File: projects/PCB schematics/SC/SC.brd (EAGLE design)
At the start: 99.1 x 99.1 mm, 76 parts, among them X1 5566-10, X2 5566-2, X4 5566-12

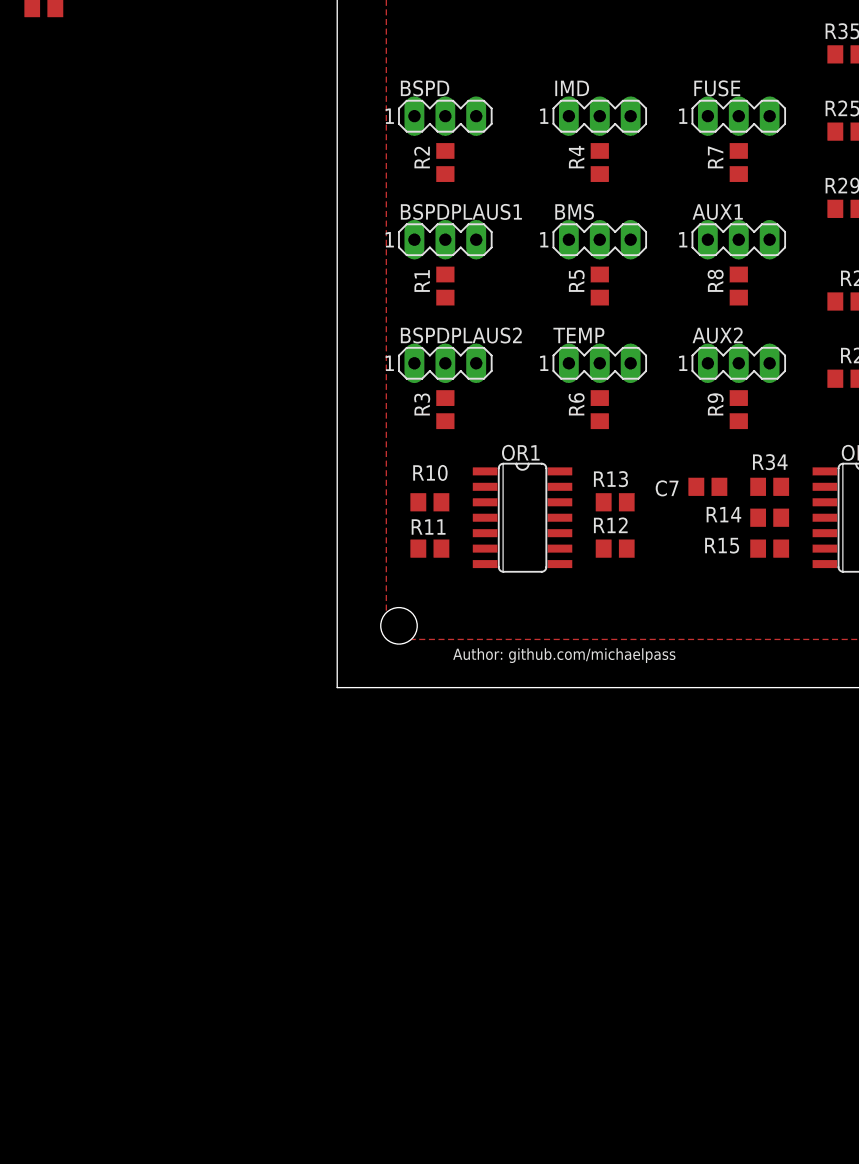
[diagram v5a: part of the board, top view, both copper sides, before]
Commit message: TEMP - Initial board placement; Horizontal redo.
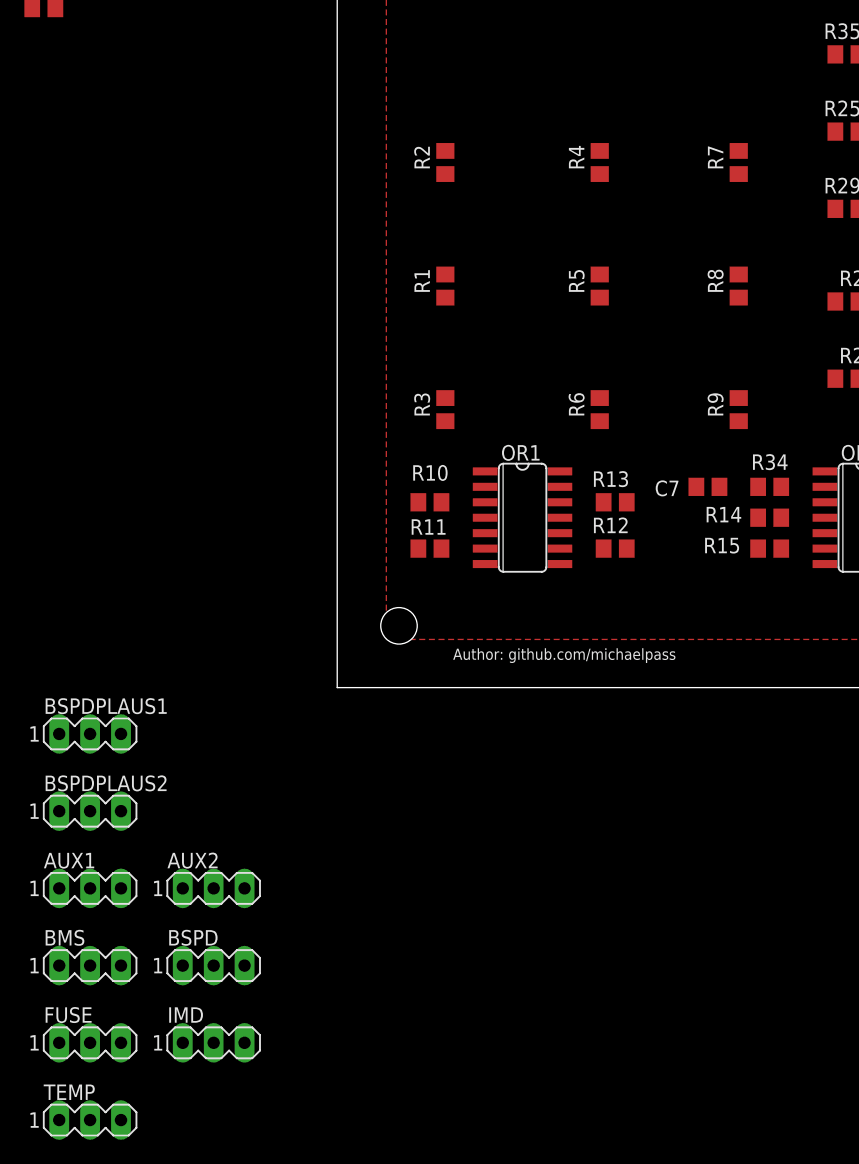
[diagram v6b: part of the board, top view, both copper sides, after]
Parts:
- moved FUSE 93.0 mm to (-20.3, -29.2)
- moved IMD 82.5 mm to (-10.2, -29.2)
- moved AUX1 75.4 mm to (-20.3, -16.5)
- moved TEMP 75.0 mm to (-20.3, -35.6)
- moved BMS 72.9 mm to (-20.3, -22.9)
- moved BSPD 72.4 mm to (-10.2, -22.9)
- moved AUX2 61.1 mm to (-10.2, -16.5)
- moved BSPDPLAUS1 50.0 mm to (-20.3, -3.81)
- moved BSPDPLAUS2 47.0 mm to (-20.3, -10.2)
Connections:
- new net GND1: AUX1.3, AUX2.3, BMS.3, BSPDPLAUS2.3, FUSE.3, IMD.3, TEMP.3
- new net N$20: BSPD.3
- net AUX1_B: no longer BUF2.4
- net AUX2_B: no longer BUF2.6
- net BMSFAULT_B: no longer BUF1.10
- net BSPDFAULT_B: no longer BUF1.2
- net BSPDPLAUS1_B: no longer BUF1.4
- net BSPDPLAUS1_O: no longer BSPDPLAUS1.2
- net BSPDPLAUS2_B: no longer BUF1.6
- net FUSEFAULT_B: no longer BUF2.2
- net GND: no longer AUX1.3, AUX2.3, BMS.3, BSPD.3, BSPDPLAUS1.3, BSPDPLAUS2.3, FUSE.3, IMD.3, TEMP.3
- net IMDFAULT_B: no longer BUF1.8
- net TEMPFAULT_B: no longer BUF1.12

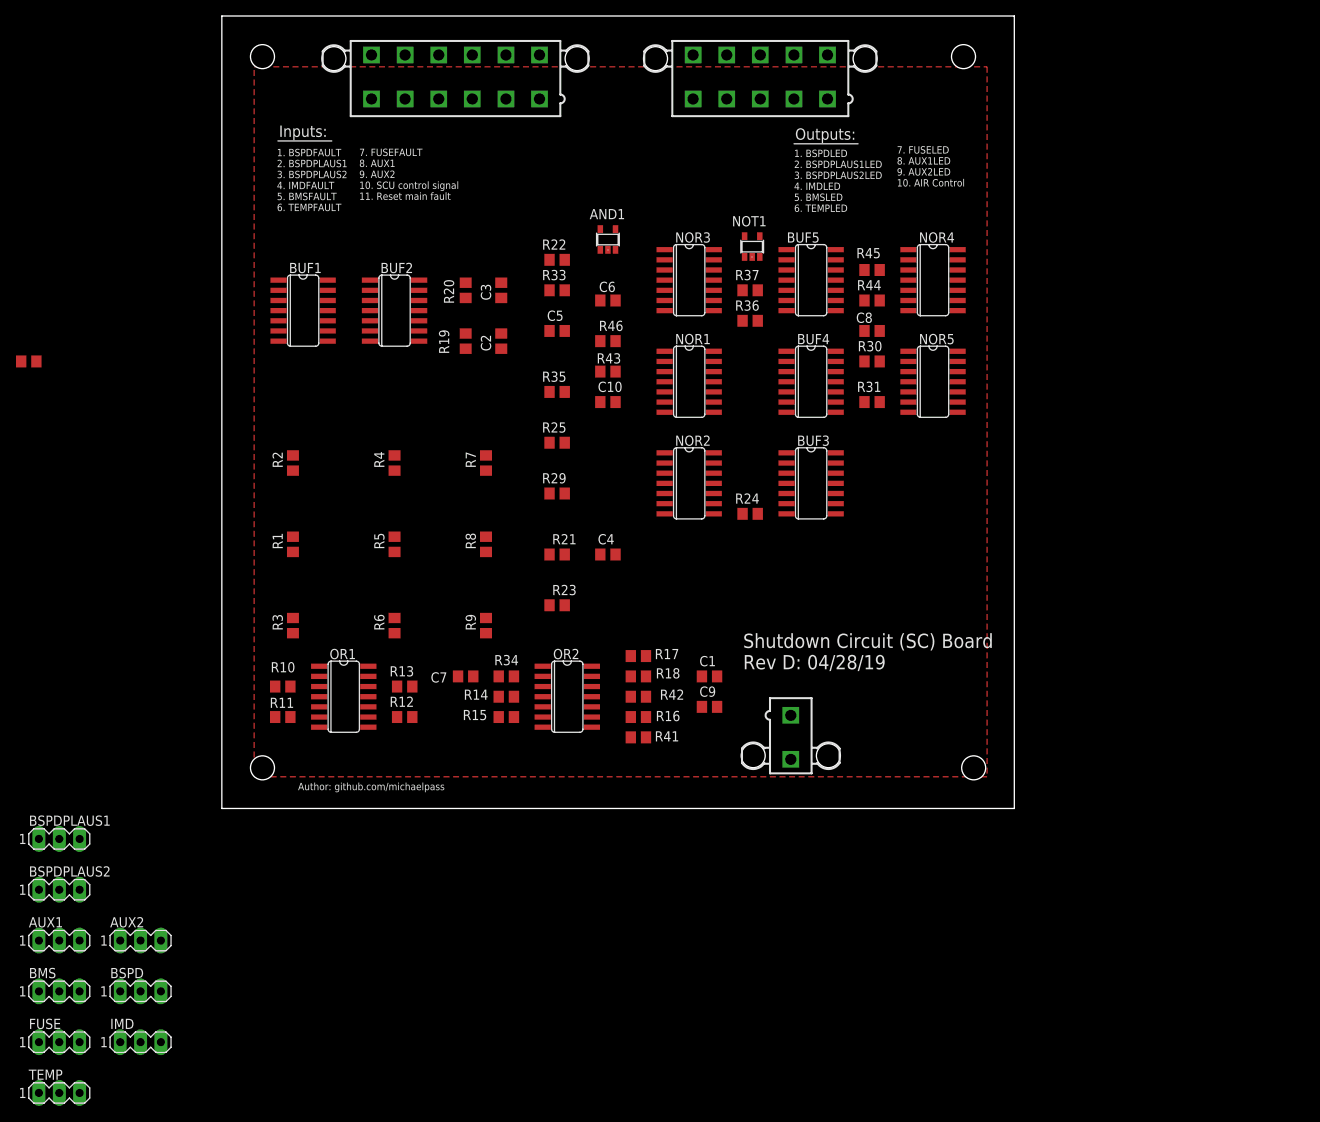
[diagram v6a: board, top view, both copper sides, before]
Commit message: SC - Hand routing. Ready for autorouter.
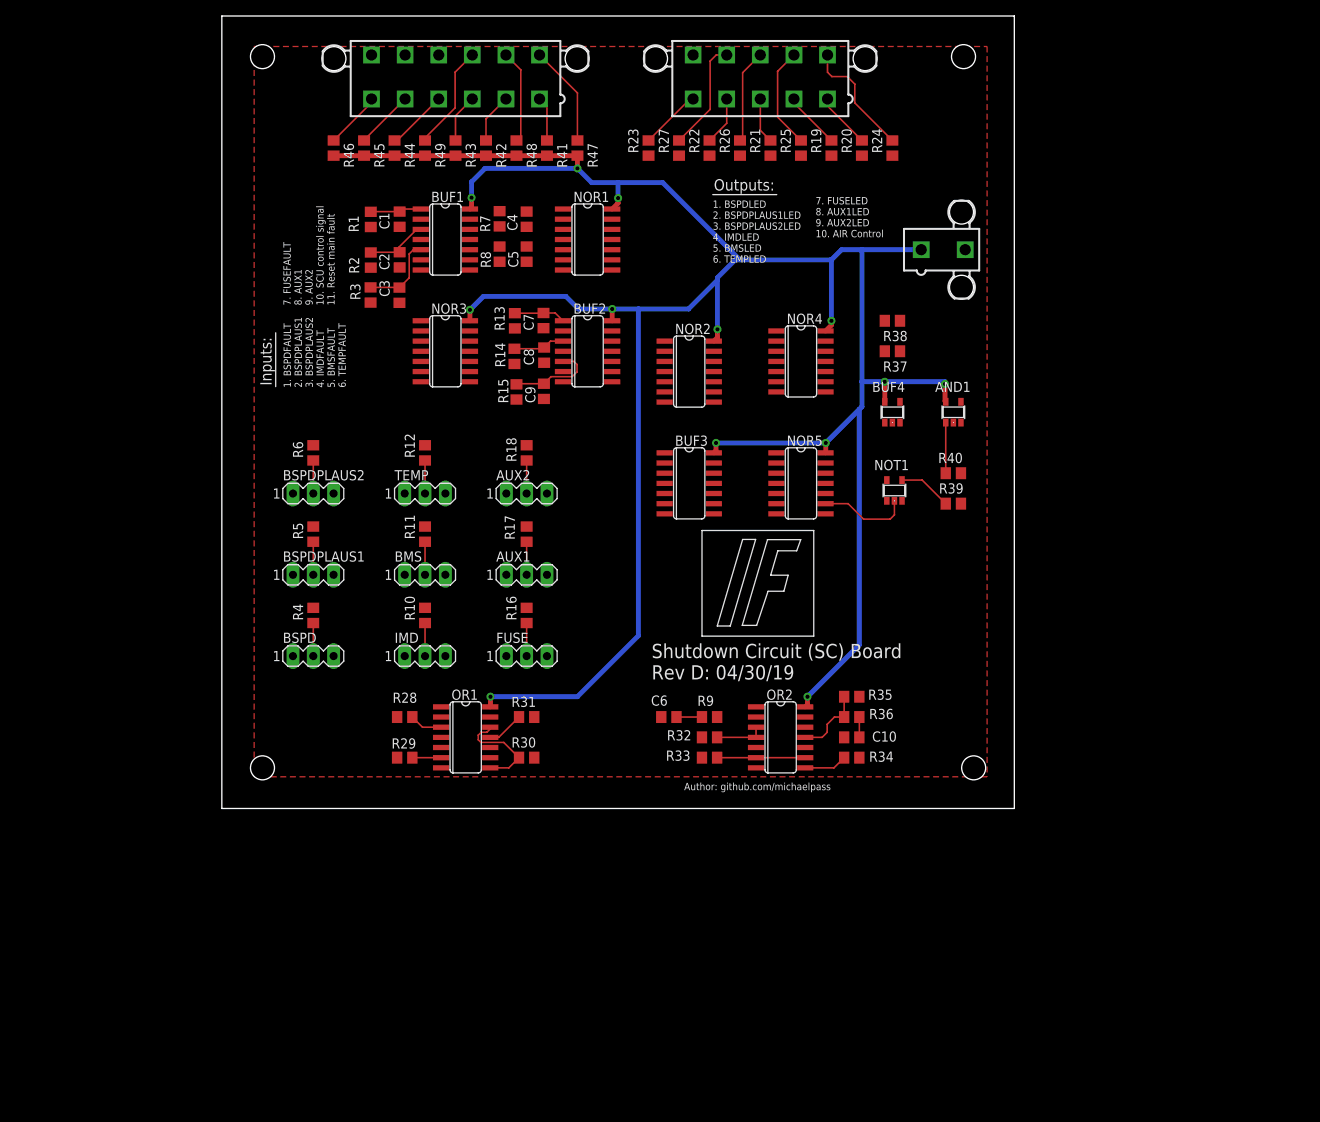
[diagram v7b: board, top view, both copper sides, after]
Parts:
- removed BUF5: 74HC7014, IowaFormula:SO14
- removed X4: 5566-12, con-molex:5566-12
- added R26, R27, R28, R38, R39, R40: 10k, rcl:R0805
- added R47, R48, R49: 47k, rcl:R0805
- added X3: 5566-10, con-molex:5566-10
- BUF4: value 74HC7014 -> 74AUC1G17DBV; device IowaFormula:SO14 -> 74xx-little-us:SOT23-5
- C1, C2, C3, C4, C5, C6, C7, C8, C9: value 1 uF -> 1u
- NOR1, NOR2, NOR3, NOR4, NOR5: value 74LS02D -> 74ALS02D
- R1, R13, R14, R15, R2, R3, R44, R45, R46, R7, R8, R9: value 10k -> 47k
- R18, R19, R20, R21, R32, R33, R34: value 50k -> 10k
- R36: value 10k -> 50k
- R41, R42, R43: value 50k -> 47k
- X1: value 5566-10 -> 5566-2; device con-molex:5566-10 -> con-molex:5566-2
- X2: value 5566-2 -> 5566-12; device con-molex:5566-2 -> con-molex:5566-12
- moved R32 97.2 mm to (61.0, 8.89), turned to 0 degrees
- moved X2 92.6 mm to (29.2, 91.4), turned to 0 degrees
- moved TEMP 87.8 mm to (25.4, 39.4)
- moved FUSE 75.8 mm to (38.1, 19.1)
- moved R41 74.5 mm to (40.6, 82.5), turned to 270 degrees
- moved AUX1 74.2 mm to (38.1, 29.2)
- moved AUX2 73.8 mm to (38.1, 39.4)
- moved R42 71.2 mm to (33.0, 82.5), turned to 270 degrees
- moved BMS 69.3 mm to (25.4, 29.2)
- moved C1 69.0 mm to (22.2, 73.7), turned to 270 degrees
- moved R30 65.7 mm to (38.1, 6.35)
- moved R45 65.3 mm to (17.8, 82.5), turned to 270 degrees
- moved R44 62.7 mm to (21.6, 82.5), turned to 270 degrees
- moved R33 61.4 mm to (61.0, 6.35), turned to 0 degrees
- moved IMD 59.9 mm to (25.4, 19.1)
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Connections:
- removed net AUX1_O: AUX1.2, OR2.10, R8.2
- removed net AUX2_O: AUX2.2, OR2.13, R9.2
- removed net BMSFAULT_O: BMS.2, OR1.13, R5.2
- removed net BSPDFAULT_O: BSPD.2, OR1.1, R2.2
- removed net BSPDPLAUS1_O: OR1.2, R1.2
- removed net BSPDPLAUS2_O: BSPDPLAUS2.2, OR1.5, R3.2
- removed net FUSEFAULT_O: FUSE.2, OR2.5, R7.2
- removed net GND1: AUX1.3, AUX2.3, BMS.3, BSPDPLAUS2.3, FUSE.3, IMD.3, TEMP.3
- removed net IMDFAULT_O: IMD.2, OR1.10, R4.2
- removed net N$20: BSPD.3
- removed net TEMPFAULT_O: OR2.2, R6.2, TEMP.2
- net AIR_CONTROL: now also X3.10; no longer X1.10
- net AUX1: now also R14.1, R48.1, X2.8; no longer R42.1, X4.8
- net AUX1_B: now also BUF2.4
- net AUX1_LED: now also BUF3.10, OR2.10, R26.2, X3.8; no longer BUF2.3, BUF4.2, X1.8
- net AUX2: now also R15.1, R49.1, X2.9; no longer R43.1, X4.9
- net AUX2_B: now also BUF2.6
- net AUX2_LED: now also BUF3.12, OR2.13, R27.2, X3.9; no longer BUF2.5, BUF4.6, X1.9
- net BMSFAULT: now also R45.1, R8.1, X2.5; no longer R33.1, X4.5
- net BMSFAULT_B: now also BUF1.10
- net BMSFAULT_LED: now also BUF3.4, OR1.13, R23.2, X3.5; no longer BUF1.11, BUF5.2, X1.5
- net BSPDFAULT: now also R1.1, R41.1, X2.1; no longer R19.1, X4.1
- net BSPDFAULT_B: now also BUF1.2
- net BSPDFAULT_LED: now also BUF2.8, OR1.1, R20.2, X3.1; no longer BUF1.1, BUF2.10, X1.1
- net BSPDPLAUS1: now also R2.1, R42.1, X2.2; no longer R20.1, X4.2
- net BSPDPLAUS1_B: now also BUF1.4
- net BSPDPLAUS1_LED: now also BUF2.10, OR1.2, R19.2, X3.2; no longer BUF1.3, BUF3.2, X1.2
- net BSPDPLAUS2: now also R3.1, R43.1, X2.3; no longer R21.1, X4.3
- net BSPDPLAUS2_B: now also BUF1.6
- net BSPDPLAUS2_LED: now also BUF2.12, OR1.5, R21.2, X3.3; no longer BUF1.5, BUF3.6, X1.3
- net FUSEFAULT: now also R13.1, R47.1, X2.7; no longer R41.1, X4.7
- net FUSEFAULT_B: now also BUF2.2
- net FUSEFAULT_LED: now also BUF3.8, OR2.5, R25.2, X3.7; no longer BUF2.1, BUF5.10, X1.7
- net GND: now also AUX1.3, AUX2.3, BMS.3, BSPD.3, BSPDPLAUS1.3, BSPDPLAUS2.3, BUF4.3, FUSE.3, IMD.3, R18.1, R19.1, R20.1, R21.1, R26.1, R27.1, R28.1, R32.1, R33.1, R34.1, R38.1, R39.1, R40.1, TEMP.3, X1.2; no longer BUF4.7, BUF5.7, R1.1, R13.1, R14.1, R15.1, R2.1, R3.1, R36.1, R44.1, R45.1, R46.1, R7.1, R8.1, R9.1, X2.2
- net IMDFAULT: now also R44.1, R7.1, X2.4; no longer R32.1, X4.4
- net IMDFAULT_B: now also BUF1.8
- net IMDFAULT_LED: now also BUF3.2, OR1.10, R22.2, X3.4; no longer BUF1.9, BUF3.10, X1.4
- net N$1: now also R33.2; no longer R15.2
- net N$10: now also BUF1.13, C6.1, R9.2; no longer BUF5.3, C7.1, R34.2
- net N$11: now also R35.2, R36.1; no longer R17.2, R18.1
- net N$12: now also R29.2; no longer R11.2
- net N$13: now also R30.2; no longer R12.2
- net N$14: now also R31.2; no longer R13.2
- net N$15: now also BUF2.1, C7.1, R13.2; no longer BUF5.9, C8.1, R41.2
- net N$16: now also BUF2.3, C8.1, R14.2; no longer BUF5.13, C9.1, R42.2
- net N$17: now also R32.2; no longer R14.2
- net N$18: now also BUF1.1, C1.1, R1.2; no longer BUF2.9, C2.1, R19.2
- net N$19: now also BUF2.5, C9.1, R15.2; no longer BUF4.3, C10.1, R43.2
- net N$2: now also R34.2; no longer R16.2
- net N$3: now also R28.2; no longer R10.2
- net N$4: now also BUF1.3, C2.1, R2.2; no longer BUF2.13, C3.1, R20.2
- net N$5: now also BUF1.5, C3.1, R3.2; no longer BUF3.3, C4.1, R21.2
- net N$6: now also BUF4.2, C10.1, R36.2; no longer BUF4.9, C1.1, R18.2
- net N$7: now also BUF1.9, C4.1, R7.2; no longer BUF3.9, C5.1, R32.2
- net N$8: now also R39.2; no longer R30.2
- net N$9: now also BUF1.11, C5.1, R8.2; no longer BUF3.13, C6.1, R33.2
- net Q: now also NOR5.13, NOR5.9; no longer NOR1.3, NOR1.4
- net Q_AUX1: now also BUF3.11, NOR4.13, NOR4.9; no longer BUF4.1, NOR5.3, NOR5.4
- net Q_AUX2: now also BUF3.13, NOR5.3, NOR5.4; no longer BUF4.5, NOR5.13, NOR5.9
- net Q_BMSFAULT: now also BUF3.3, NOR3.3, NOR3.4; no longer BUF5.1, NOR3.13, NOR3.9
- net Q_BSPDFAULT: now also BUF2.9, NOR1.3, NOR1.4; no longer BUF2.11, NOR1.13, NOR1.9
- net Q_BSPDPLAUS1: now also BUF2.11, NOR1.13, NOR1.9; no longer BUF3.1, NOR2.3, NOR2.4
- net Q_BSPDPLAUS2: now also BUF2.13, NOR2.3, NOR2.4; no longer BUF3.5, NOR2.13, NOR2.9
- net Q_FUSEFAULT: now also BUF3.9, NOR4.3, NOR4.4; no longer BUF5.11, NOR4.13, NOR4.9
- net Q_IMDFAULT: now also BUF3.1, NOR2.13, NOR2.9; no longer BUF3.11, NOR3.3, NOR3.4
- net Q_TEMPFAULT: now also BUF3.5, NOR3.13, NOR3.9; no longer BUF5.5, NOR4.3, NOR4.4
- net RESET_MAINFAULT: now also R38.2, X2.11; no longer R29.2, X4.11
- net SCU_CONTROL: now also R40.2, X2.10; no longer R31.2, X4.10
- net SET_AUX1: now also AUX1.2, NOR4.8, R17.2; no longer BUF5.12, NOR5.2, R45.2
- net SET_AUX2: now also AUX2.2, NOR5.2, R18.2; no longer BUF4.4, NOR5.8, R46.2
- net SET_BMSFAULT: now also BMS.2, NOR3.2, R11.2; no longer BUF3.12, NOR3.8, R36.2
- net SET_BSPDFAULT: now also BSPD.2, NOR1.2, R4.2; no longer BUF2.8, NOR1.8, R22.2
- net SET_BSPDPLAUS1: now also BSPDPLAUS1.2, NOR1.8, R5.2; no longer BUF2.12, NOR2.2, R23.2
- net SET_BSPDPLAUS2: now also BSPDPLAUS2.2, NOR2.2, R6.2; no longer BUF3.4, NOR2.8, R24.2
- net SET_FUSEFAULT: now also FUSE.2, NOR4.2, R16.2; no longer BUF5.8, NOR4.8, R44.2
- net SET_IMDFAULT: now also IMD.2, NOR2.8, R10.2; no longer BUF3.8, NOR3.2, R35.2
- net SET_MAINFAULT: now also BUF4.4, NOR5.8, R37.2; no longer BUF4.8, NOR1.2, R25.2
- net SET_TEMPFAULT: now also NOR3.8, R12.2, TEMP.2; no longer BUF5.4, NOR4.2, R37.2
- net TEMPFAULT: now also R46.1, R9.1, X2.6; no longer R34.1, X4.6
- net TEMPFAULT_B: now also BUF1.12
- net TEMPFAULT_LED: now also BUF3.6, OR2.2, R24.2, X3.6; no longer BUF1.13, BUF5.6, X1.6
- net VCC: now also BUF4.5, R41.2, R42.2, R43.2, R44.2, R45.2, R46.2, R47.2, R48.2, R49.2, X1.1; no longer BUF4.14, BUF5.14, X2.1
- net ~Q: now also NOR5.10, NOR5.11; no longer NOR1.1, NOR1.5
- net ~Q_AUX1: now also NOR4.10, NOR4.11; no longer NOR5.1, NOR5.5
- net ~Q_AUX2: now also NOR5.1, NOR5.5; no longer NOR5.10, NOR5.11
- net ~Q_BMSFAULT: now also NOR3.1, NOR3.5; no longer NOR3.10, NOR3.11
- net ~Q_BSPDFAULT: now also NOR1.1, NOR1.5; no longer NOR1.10, NOR1.11
- net ~Q_BSPDPLAUS1: now also NOR1.10, NOR1.11; no longer NOR2.1, NOR2.5
- net ~Q_BSPDPLAUS2: now also NOR2.1, NOR2.5; no longer NOR2.10, NOR2.11
- net ~Q_FUSEFAULT: now also NOR4.1, NOR4.5; no longer NOR4.10, NOR4.11
- net ~Q_IMDFAULT: now also NOR2.10, NOR2.11; no longer NOR3.1, NOR3.5
- net ~Q_TEMPFAULT: now also NOR3.10, NOR3.11; no longer NOR4.1, NOR4.5
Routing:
- net VCC: track 0.00 -> 320.6 mm, vias 0 -> 13
- net TEMPFAULT_LED: track 0.00 -> 15.2 mm
- net AUX2_LED: track 0.00 -> 13.9 mm
- net AUX2: track 0.00 -> 13.1 mm
- net N$13: track 0.00 -> 12.8 mm
- net FUSEFAULT_LED: track 0.00 -> 12.7 mm
- net FUSEFAULT: track 0.00 -> 12.7 mm
- net AUX1_LED: track 0.00 -> 11.7 mm
- net AUX1: track 0.00 -> 11.7 mm
- net Q: track 0.00 -> 11.4 mm
- net N$19: track 0.00 -> 11.1 mm
- net N$1: track 0.00 -> 11.0 mm
- net N$5: track 0.00 -> 10.00 mm
- net N$11: track 0.00 -> 9.04 mm
- net N$4: track 0.00 -> 7.91 mm
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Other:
- board text added: "Shutdown Circuit (SC) Board Rev D: 04/30/19"
- board text removed: "Shutdown Circuit (SC) Board Rev D: 04/28/19"

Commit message: SC - Final revision D.
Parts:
- moved NOR2 1.27 mm to (58.4, 55.9)
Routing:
- net BSPDPLAUS1_LED: track 7.13 -> 222.3 mm, vias 0 -> 2
- net BSPDFAULT_LED: track 6.97 -> 214.2 mm, vias 0 -> 3
- net RESET_MAINFAULT: track 0.00 -> 177.4 mm, vias 0 -> 10
- net AUX2_LED: track 13.9 -> 166.8 mm, vias 0 -> 2
- net TEMPFAULT: track 7.15 -> 155.7 mm
- net TEMPFAULT_LED: track 15.2 -> 162.4 mm, vias 0 -> 3
- net N$10: track 3.18 -> 145.4 mm, vias 0 -> 2
- net FUSEFAULT_LED: track 12.7 -> 151.7 mm, vias 0 -> 3
- net SCU_CONTROL: track 6.33 -> 132.3 mm
- net AUX1_LED: track 11.7 -> 124.2 mm, vias 0 -> 3
- net GND: track 0.00 -> 108.3 mm, vias 0 -> 21
- net BSPDPLAUS2_LED: track 5.72 -> 110.5 mm, vias 0 -> 3
- net IMDFAULT_LED: track 6.08 -> 110.0 mm, vias 0 -> 4
- net SET_BSPDFAULT: track 4.13 -> 102.8 mm, vias 0 -> 1
- net BMSFAULT_LED: track 7.72 -> 101.5 mm, vias 0 -> 2
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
